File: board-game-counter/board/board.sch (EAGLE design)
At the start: 42 parts, among them IC1 TINY13-20PU, IC2 74HCT595N, IC3 74HCT595N, T1 A42, T2 A42, T3 A42, T4 A42, T5 S9013

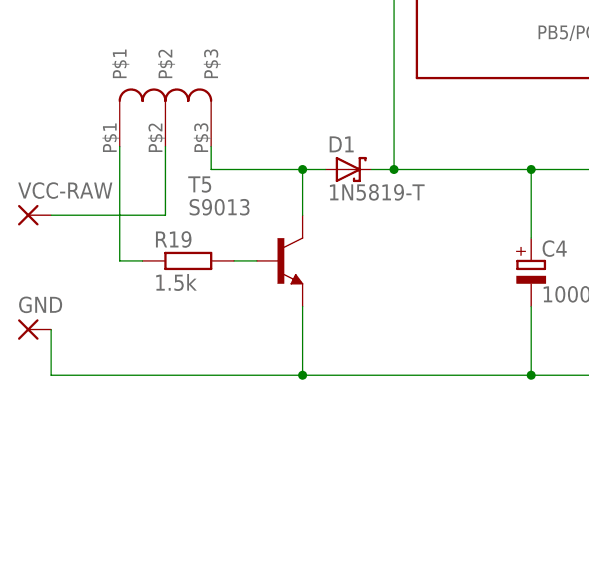
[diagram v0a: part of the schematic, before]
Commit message: board-game-counter updated
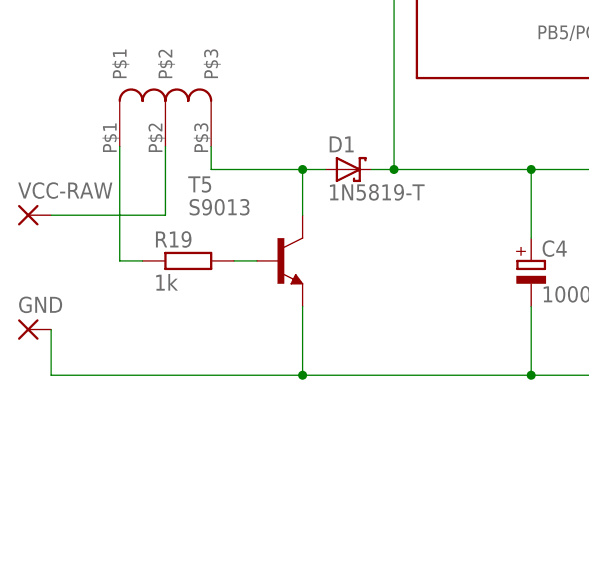
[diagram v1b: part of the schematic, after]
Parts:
- R19: value 1.5k -> 1k
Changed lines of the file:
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@@
 <grid distance="0.1" unitdist="inch" unit="inch" style="lines" multiple="1" display="no" altdistance="0.01" altunitdist="inch" altunit="inch"/>
 <layers>
-<layer number="1" name="Top" color="4" fill="1" visible="yes" active="no"/>
-<layer number="16" name="Bottom" color="1" fill="1" visible="yes" active="no"/>
-<layer number="17" name="Pads" color="2" fill="1" visible="yes" active="no"/>
-<layer number="18" name="Vias" color="2" fill="1" visible="yes" active="no"/>
-<layer number="19" name="Unrouted" color="6" fill="1" visible="yes" active="no"/>
-<layer number="20" name="Dimension" color="24" fill="1" visible="yes" active="no"/>
-<layer number="21" name="tPlace" color="7" fill="1" visible="yes" active="no"/>
-<layer number="22" name="bPlace" color="7" fill="1" visible="yes" active="no"/>
-<layer number="23" name="tOrigins" color="15" fill="1" visible="yes" active="no"/>
-<layer number="24" name="bOrigins" color="15" fill="1" visible="yes" active="no"/>
-<layer number="25" name="tNames" color="7" fill="1" visible="yes" active="no"/>
-<layer number="26" name="bNames" color="7" fill="1" visible="yes" active="no"/>
-<layer number="27" name="tValues" color="7" fill="1" visible="yes" active="no"/>
-<layer number="28" name="bValues" color="7" fill="1" visible="yes" active="no"/>
+<layer number="1" name="Top" color="4" fill="1" visible="no" active="no"/>
+<layer number="16" name="Bottom" color="1" fill="1" visible="no" active="no"/>
+<layer number="17" name="Pads" color="2" fill="1" visible="no" active="no"/>
+<layer number="18" name="Vias" color="2" fill="1" visible="no" active="no"/>
+<layer number="19" name="Unrouted" color="6" fill="1" visible="no" active="no"/>
+<layer number="20" name="Dimension" color="24" fill="1" visible="no" active="no"/>
+<layer number="21" name="tPlace" color="7" fill="1" visible="no" active="no"/>
+<layer number="22" name="bPlace" color="7" fill="1" visible="no" active="no"/>
+<layer number="23" name="tOrigins" color="15" fill="1" visible="no" active="no"/>
+<layer number="24" name="bOrigins" color="15" fill="1" visible="no" active="no"/>
+<layer number="25" name="tNames" color="7" fill="1" visible="no" active="no"/>
+<layer number="26" name="bNames" color="7" fill="1" visible="no" active="no"/>
+<layer number="27" name="tValues" color="7" fill="1" visible="no" active="no"/>
+<layer number="28" name="bValues" color="7" fill="1" visible="no" active="no"/>
 <layer number="29" name="tStop" color="7" fill="3" visible="no" active="no"/>
 <layer number="30" name="bStop" color="7" fill="6" visible="no" active="no"/>
@@
 <layer number="35" name="tGlue" color="7" fill="4" visible="no" active="no"/>
 <layer number="36" name="bGlue" color="7" fill="5" visible="no" active="no"/>
-<layer number="37" name="tTest" color="7" fill="1" visible="yes" active="no"/>
-<layer number="38" name="bTest" color="7" fill="1" visible="yes" active="no"/>
+<layer number="37" name="tTest" color="7" fill="1" visible="no" active="no"/>
+<layer number="38" name="bTest" color="7" fill="1" visible="no" active="no"/>
 <layer number="39" name="tKeepout" color="4" fill="11" visible="no" active="no"/>
 <layer number="40" name="bKeepout" color="1" fill="11" visible="no" active="no"/>
@@
 <layer number="44" name="Drills" color="7" fill="1" visible="no" active="no"/>
 <layer number="45" name="Holes" color="7" fill="1" visible="no" active="no"/>
-<layer number="46" name="Milling" color="3" fill="1" visible="yes" active="no"/>
-<layer number="47" name="Measures" color="7" fill="1" visible="yes" active="no"/>
-<layer number="48" name="Document" color="7" fill="1" visible="yes" active="no"/>
-<layer number="49" name="Reference" color="7" fill="1" visible="yes" active="no"/>
-<layer number="51" name="tDocu" color="7" fill="1" visible="yes" active="no"/>
-<layer number="52" name="bDocu" color="7" fill="1" visible="yes" active="no"/>
+<layer number="46" name="Milling" color="3" fill="1" visible="no" active="no"/>
+<layer number="47" name="Measures" color="7" fill="1" visible="no" active="no"/>
+<layer number="48" name="Document" color="7" fill="1" visible="no" active="no"/>
+<layer number="49" name="Reference" color="7" fill="1" visible="no" active="no"/>
+<layer number="51" name="tDocu" color="7" fill="1" visible="no" active="no"/>
+<layer number="52" name="bDocu" color="7" fill="1" visible="no" active="no"/>
 <layer number="90" name="Modules" color="5" fill="1" visible="yes" active="yes"/>
 <layer number="91" name="Nets" color="2" fill="1" visible="yes" active="yes"/>
@@
 <part name="5.1V" library="diode" library_urn="urn:adsk.eagle:library:210" deviceset="1N4728" device="" package3d_urn="urn:adsk.eagle:package:43341/1"/>
 <part name="C4" library="resistor" library_urn="urn:adsk.eagle:library:348" deviceset="CPOL-EU" device="E3.5-8" package3d_urn="urn:adsk.eagle:package:25842/1" value="1000uf"/>
-<part name="R19" library="resistor" library_urn="urn:adsk.eagle:library:348" deviceset="R-EU_" device="0207/2V" package3d_urn="urn:adsk.eagle:package:25941/1" value="1.5k"/>
+<part name="R19" library="resistor" library_urn="urn:adsk.eagle:library:348" deviceset="R-EU_" device="0207/2V" package3d_urn="urn:adsk.eagle:package:25941/1" value="1k"/>
 <part name="U$3" library="mgvc" deviceset="TRANS" device=""/>
 <part name="VCC-RAW" library="wirepad" library_urn="urn:adsk.eagle:library:412" deviceset="2,54/0,8" device="" package3d_urn="urn:adsk.eagle:package:30838/1"/>
